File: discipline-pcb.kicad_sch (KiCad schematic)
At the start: 205 parts, among them SW1 KEYSW, SW10 KEYSW, SW11 KEYSW, SW12 KEYSW, SW13 KEYSW, SW14 KEYSW, SW16 KEYSW, SW17 KEYSW, SW18 KEYSW, SW19 KEYSW, SW2 KEYSW, SW20 KEYSW, SW21 KEYSW, SW22 KEYSW, SW23 KEYSW, SW24 KEYSW, SW25 KEYSW, SW26 KEYSW, SW27 KEYSW, SW28 KEYSW, SW29 KEYSW, SW3 KEYSW, SW31 KEYSW, SW32 KEYSW, SW33 KEYSW, SW34 KEYSW, SW35 KEYSW, SW36 KEYSW, SW37 KEYSW, SW38 KEYSW, SW39 KEYSW, SW4 KEYSW, SW40 KEYSW, SW41 KEYSW, SW42 KEYSW, SW43 KEYSW, SW45 KEYSW, SW46 KEYSW, SW47 KEYSW, SW48 KEYSW, SW49 KEYSW, SW5 KEYSW, SW50 KEYSW, SW51 KEYSW, SW52 KEYSW, SW53 KEYSW, SW54 KEYSW, SW55 KEYSW, SW56 KEYSW, SW57 KEYSW, SW59 KEYSW, SW6 KEYSW, SW60 KEYSW, SW61 KEYSW, SW62 KEYSW, SW7 KEYSW, SW72 KEYSW, SW73 KEYSW, SW74 KEYSW, SW75 KEYSW, SW76 KEYSW, SW77 KEYSW, SW78 KEYSW, SW79 KEYSW, SW8 KEYSW, SW80 KEYSW, SW81 KEYSW, SW82 KEYSW, SW83 KEYSW, SW9 KEYSW, U1 SN74AHCT125N

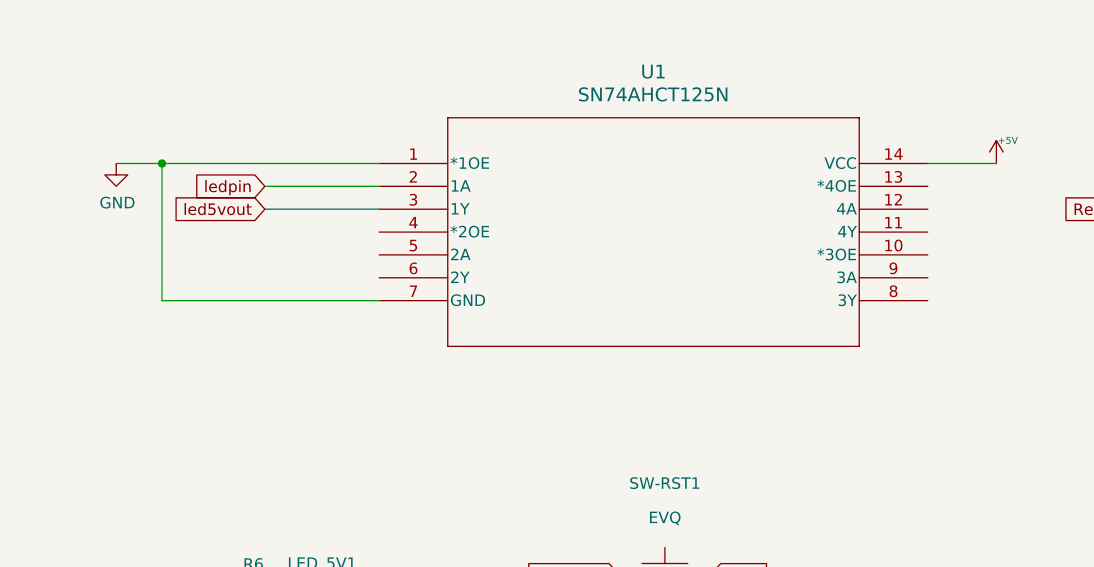
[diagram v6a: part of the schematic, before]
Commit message: add 3d model to level shifter
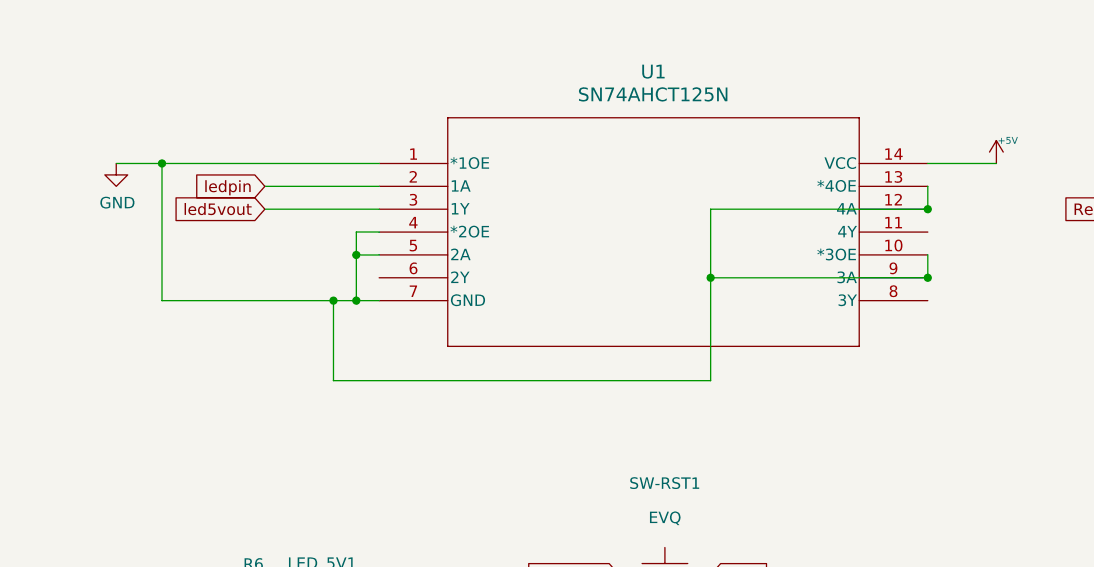
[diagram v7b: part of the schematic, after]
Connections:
- net GND: now also U1.10 (*3OE), U1.12 (4A), U1.13 (*4OE), U1.4 (*2OE), U1.5 (2A), U1.9 (3A)
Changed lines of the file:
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@@
 	)
 	(junction
+		(at 92.71 148.59)
+		(diameter 0)
+		(color 0 0 0 0)
+	)
+	(junction
 		(at 260.35 36.83)
 		(diameter 0)
@@
 	)
 	(junction
+		(at 53.34 151.13)
+		(diameter 0)
+		(color 0 0 0 0)
+	)
+	(junction
 		(at 354.33 170.18)
 		(diameter 0)
@@
 	)
 	(junction
+		(at 50.8 151.13)
+		(diameter 0)
+		(color 0 0 0 0)
+	)
+	(junction
 		(at 170.18 27.94)
 		(diameter 0)
@@
 	)
 	(junction
+		(at 53.34 146.05)
+		(diameter 0)
+		(color 0 0 0 0)
+	)
+	(junction
 		(at 276.86 27.94)
 		(diameter 0)
@@
 	)
 	(junction
+		(at 116.84 140.97)
+		(diameter 0)
+		(color 0 0 0 0)
+	)
+	(junction
 		(at 191.77 233.68)
 		(diameter 0)
@@
 	)
 	(junction
+		(at 116.84 148.59)
+		(diameter 0)
+		(color 0 0 0 0)
+	)
+	(junction
 		(at 354.33 204.47)
 		(diameter 0)
@@
 	(wire
 		(pts
+			(xy 116.84 146.05) (xy 116.84 148.59)
+		)
+		(stroke
+			(width 0)
+			(type default)
+		)
+	)
+	(wire
+		(pts
 			(xy 134.62 233.68) (xy 140.97 233.68)
 		)
@@
 	(wire
 		(pts
+			(xy 116.84 138.43) (xy 116.84 140.97)
+		)
+		(stroke
+			(width 0)
+			(type default)
+		)
+	)
+	(wire
+		(pts
+			(xy 92.71 148.59) (xy 116.84 148.59)
+		)
+		(stroke
+			(width 0)
+			(type default)
+		)
+	)
+	(wire
+		(pts
 			(xy 240.03 189.23) (xy 254 189.23)
 		)
@@
 	(wire
 		(pts
+			(xy 53.34 143.51) (xy 53.34 146.05)
+		)
+		(stroke
+			(width 0)
+			(type default)
+		)
+	)
+	(wire
+		(pts
 			(xy 135.89 36.83) (xy 153.67 36.83)
 		)
@@
 	(wire
 		(pts
-			(xy 55.88 151.13) (xy 31.75 151.13)
+			(xy 55.88 151.13) (xy 53.34 151.13)
 		)
 		(stroke
@@
 	(wire
 		(pts
+			(xy 92.71 140.97) (xy 92.71 148.59)
+		)
+		(stroke
+			(width 0)
+			(type default)
+		)
+	)
+	(wire
+		(pts
 			(xy 224.79 41.91) (xy 224.79 43.18)
 		)
@@
 	(wire
 		(pts
+			(xy 55.88 143.51) (xy 53.34 143.51)
+		)
+		(stroke
+			(width 0)
+			(type default)
+		)
+	)
+	(wire
+		(pts
 			(xy 330.2 26.67) (xy 330.2 27.94)
 		)
@@
 	(wire
 		(pts
+			(xy 53.34 151.13) (xy 50.8 151.13)
+		)
+		(stroke
+			(width 0)
+			(type default)
+		)
+	)
+	(wire
+		(pts
 			(xy 261.62 57.15) (xy 260.35 57.15)
 		)
@@
 	(wire
 		(pts
+			(xy 50.8 151.13) (xy 31.75 151.13)
+		)
+		(stroke
+			(width 0)
+			(type default)
+		)
+	)
+	(wire
+		(pts
 			(xy 135.89 57.15) (xy 135.89 58.42)
 		)
@@
 	(wire
 		(pts
+			(xy 55.88 146.05) (xy 53.34 146.05)
+		)
+		(stroke
+			(width 0)
+			(type default)
+		)
+	)
+	(wire
+		(pts
 			(xy 303.53 132.08) (xy 327.66 132.08)
 		)
@@
 	(wire
 		(pts
+			(xy 50.8 160.02) (xy 50.8 151.13)
+		)
+		(stroke
+			(width 0)
+			(type default)
+		)
+	)
+	(wire
+		(pts
 			(xy 154.94 72.39) (xy 153.67 72.39)
 		)
@@
 	(wire
 		(pts
+			(xy 92.71 160.02) (xy 50.8 160.02)
+		)
+		(stroke
+			(width 0)
+			(type default)
+		)
+	)
+	(wire
+		(pts
 			(xy 332.74 27.94) (xy 331.47 27.94)
 		)
@@
 	(wire
 		(pts
+			(xy 53.34 146.05) (xy 53.34 151.13)
+		)
+		(stroke
+			(width 0)
+			(type default)
+		)
+	)
+	(wire
+		(pts
 			(xy 134.62 238.76) (xy 140.97 238.76)
 		)
@@
 	(wire
 		(pts
+			(xy 116.84 140.97) (xy 92.71 140.97)
+		)
+		(stroke
+			(width 0)
+			(type default)
+		)
+	)
+	(wire
+		(pts
 			(xy 193.04 163.83) (xy 194.31 163.83)
 		)
@@
 		)
 		(stroke
+			(width 0)
+			(type default)
+		)
+	)
+	(wire
+		(pts
+			(xy 92.71 148.59) (xy 92.71 160.02)
+		)
+		(stroke
